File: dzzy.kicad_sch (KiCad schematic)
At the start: 96 parts, among them J1 JTAG/SWD, P1 PC, U1 USBLC6-2SC6, U2 XC6206P332MR, U3 M95512-WMN6P, U4 GD32VF103CBT6

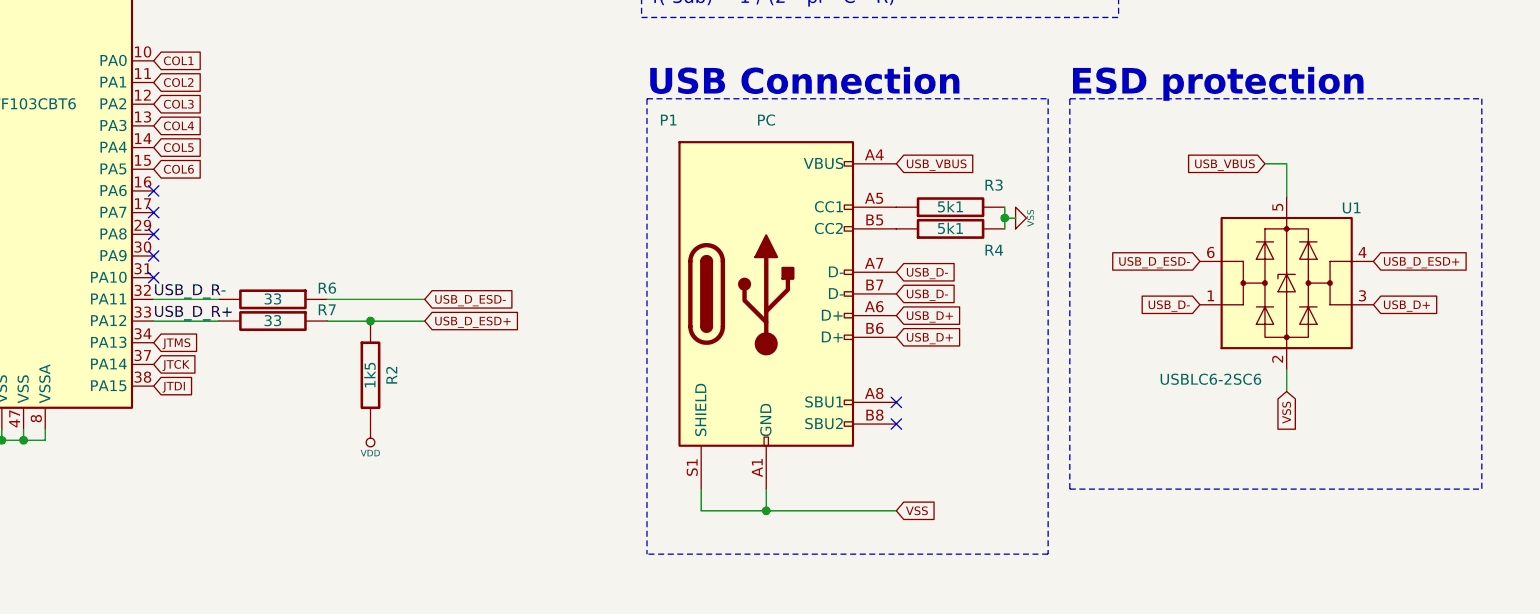
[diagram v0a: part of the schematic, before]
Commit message: Update ESD diode placement and silkscreen
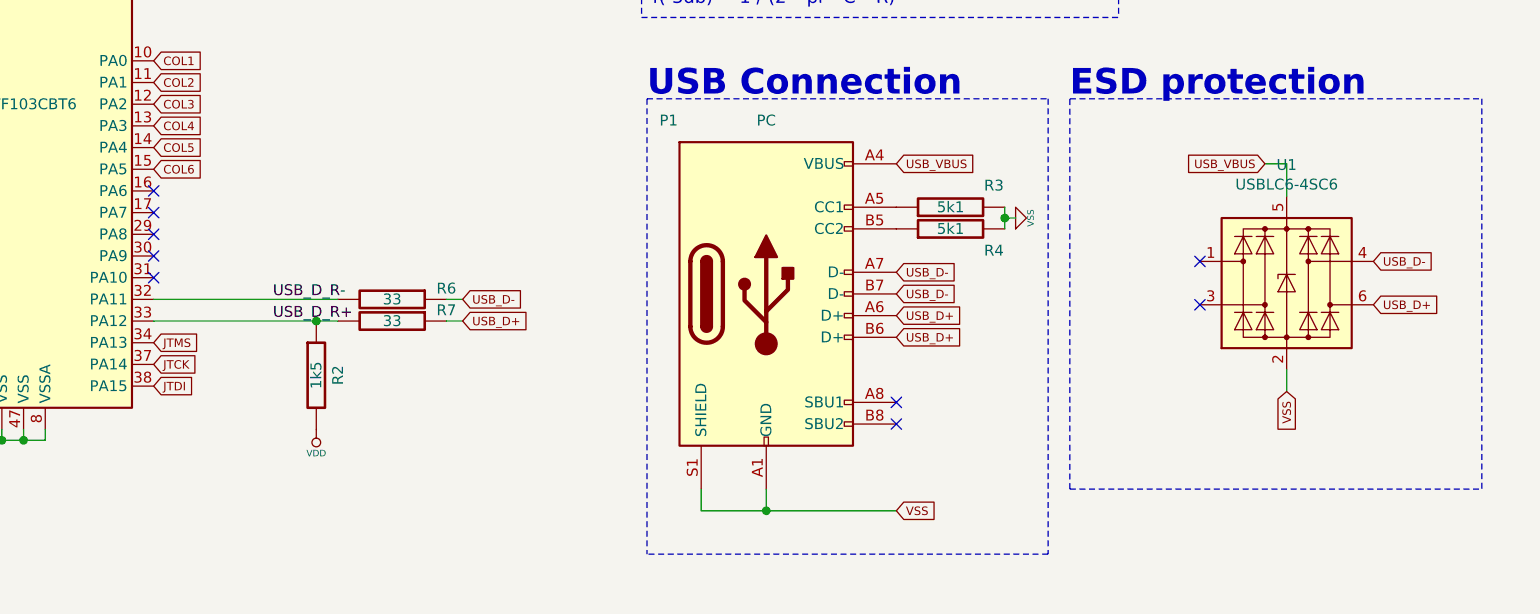
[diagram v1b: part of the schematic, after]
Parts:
- removed U1: USBLC6-2SC6, prettylib:SOT-23-6, symbol Power_Protection:USBLC6-2SC6
- added U1: USBLC6-4SC6, prettylib:SOT-23-6_flipable, symbol Power_Protection:USBLC6-4SC6
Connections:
- net USB_D_ESD- is gone; now on net USB_D-: R6.1
- net USB_D+: now also R7.1, U1.6 (I/O4)
- net USB_D-: now also U1.4 (I/O3)
- net USB_D_R+: now also R2.1
- net USB_VBUS: now also U1.5 (VBUS)
- net VSS: now also U1.2 (GND)
- removed net USB_D_ESD+: R2.1, R7.1
- no-connect marks 16 -> 18
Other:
- moved on the sheet: R2, R6, R7
